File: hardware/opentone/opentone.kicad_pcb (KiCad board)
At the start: 2 copper layers, 161.1 x 143.3 mm, 33 parts, among them J101 POWER, J102 UART, J103 DEBUG, J104 USB, SW101 PWR, SW102 RST, U1 STM32F446RCTx, U101 FSC-BT1035

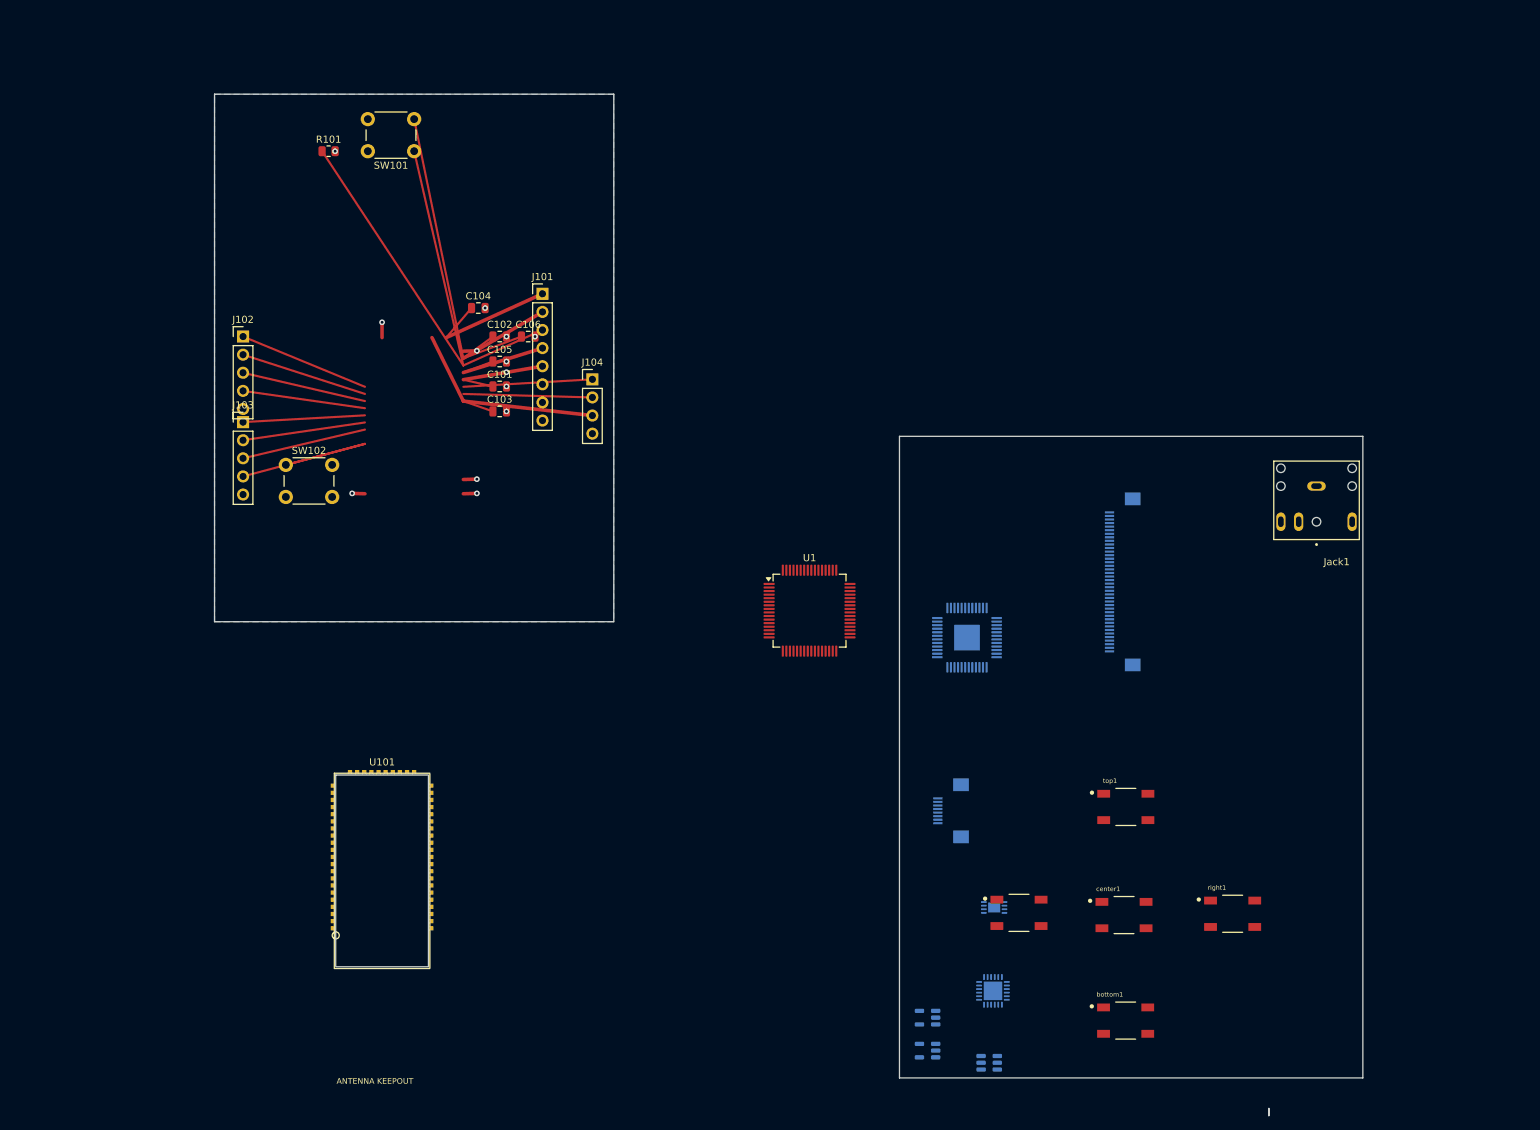
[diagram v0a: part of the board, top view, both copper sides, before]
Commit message: updated buttons and MCU
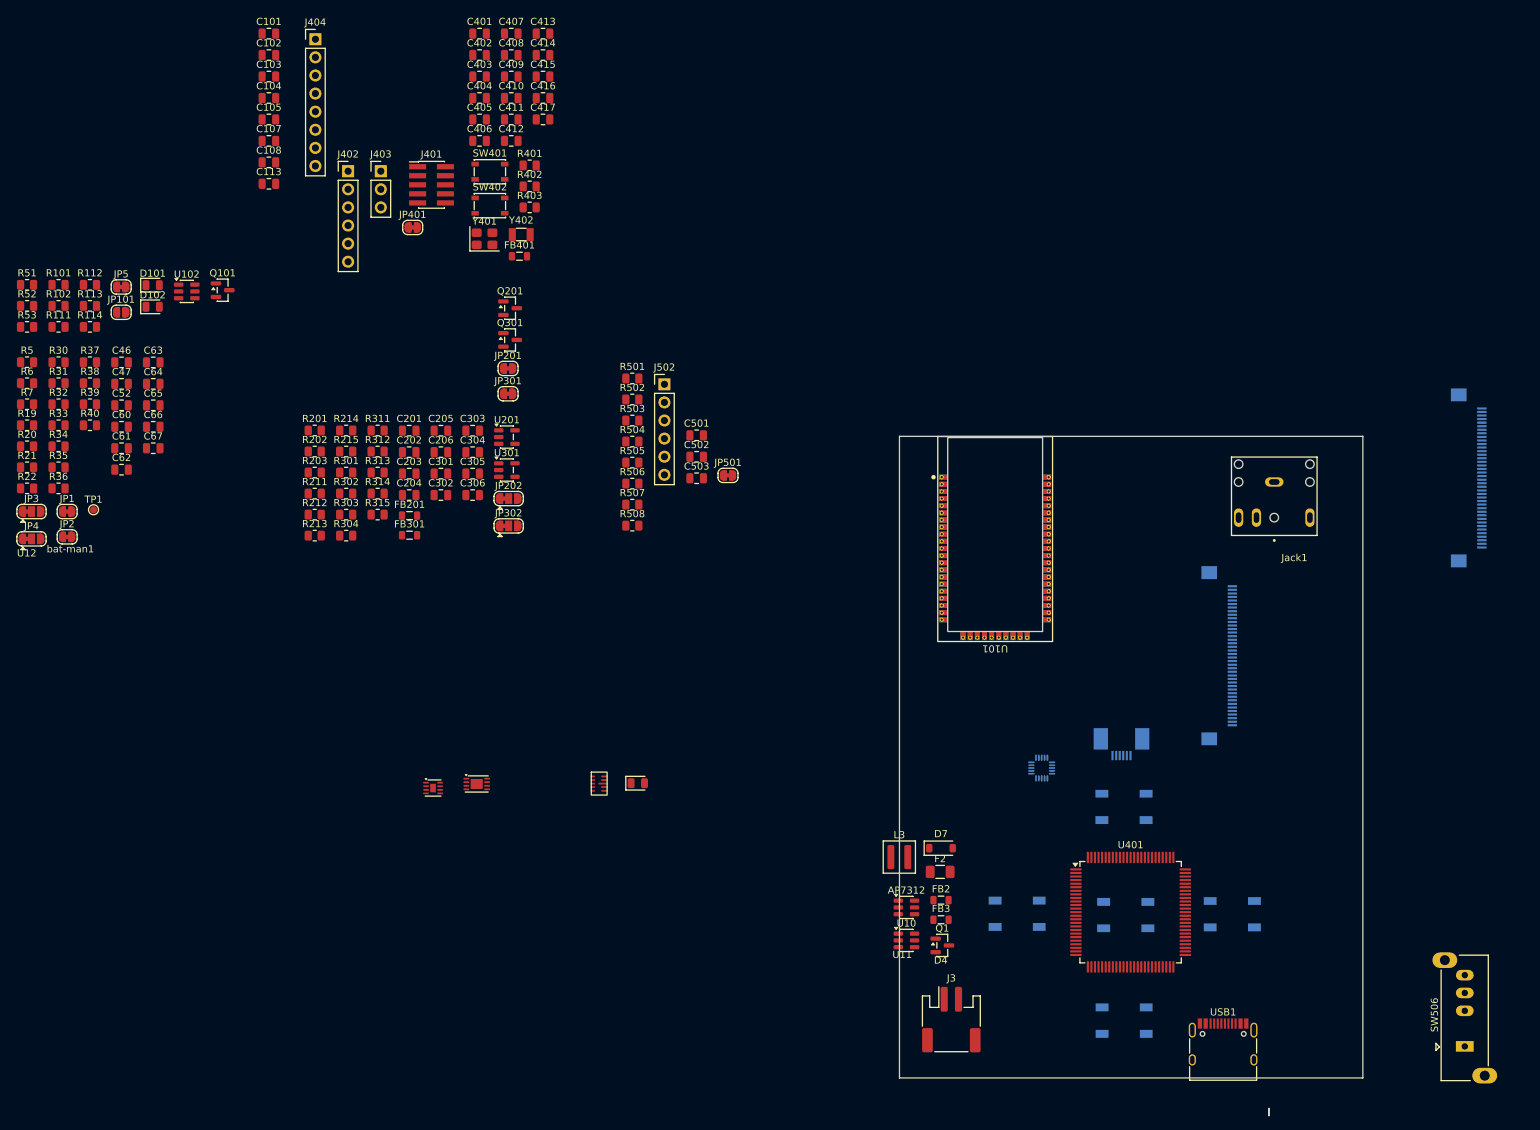
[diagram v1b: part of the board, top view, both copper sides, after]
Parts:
- removed Audiocodec1: VS1063, Package_QFP:LQFP-48-1EP_7x7mm_P0.5mm_EP3.6x3.6mm
- removed Buck-converter2: LM3671, Package_TO_SOT_SMD:TSOT-23-5
- removed C106: 10u, Capacitor_SMD:C_0805_2012Metric
- removed J101: POWER, Connector_PinHeader_2.54mm:PinHeader_1x08_P2.54mm_Vertical
- removed J102: UART, Connector_PinHeader_2.54mm:PinHeader_1x05_P2.54mm_Vertical
- removed J103: DEBUG, Connector_PinHeader_2.54mm:PinHeader_1x05_P2.54mm_Vertical
- removed J104: USB, Connector_PinHeader_2.54mm:PinHeader_1x04_P2.54mm_Vertical
- removed LDO2: MIC5504-3.3YM5, Package_TO_SOT_SMD:SOT-23-5
- removed SW101: PWR, Button_Switch_THT:SW_PUSH_6mm_H4.3mm
- removed SW102: RST, Button_Switch_THT:SW_PUSH_6mm_H4.3mm
- removed S_CONNECTOR1: ~, opentone:Hirose_FH12-40S-0.5SH_1x40-1MP_P0.50mm_Horizontal
- removed U1: STM32F446RCTx, Package_QFP:LQFP-64_10x10mm_P0.5mm
- removed UART_BRIDGE1: CP2102N-Axx-xQFN24, Package_DFN_QFN:QFN-24-1EP_4x4mm_P0.5mm_EP2.6x2.6mm
- removed clickwheel-connector2: ~, Connector_FFC-FPC:Hirose_FH12-8S-0.5SH_1x08-1MP_P0.50mm_Horizontal
- removed left1: SKQGAFE010, opentone:SW_SKQGAFE010
- added C107: 1u, Capacitor_SMD:C_0805_2012Metric, F.Cu at (11.6, 8.55)
- added C108: 1n, Capacitor_SMD:C_0805_2012Metric, F.Cu at (11.6, 11.6)
- added C113: 1u, Capacitor_SMD:C_0805_2012Metric, F.Cu at (11.6, 14.6)
- added C201: 10u, Capacitor_SMD:C_0805_2012Metric, F.Cu at (31.3, 49.2)
- added C202: 100n, Capacitor_SMD:C_0805_2012Metric, F.Cu at (31.3, 52.2)
- added C203: 10u, Capacitor_SMD:C_0805_2012Metric, F.Cu at (31.3, 55.2)
- added C204: 100n, Capacitor_SMD:C_0805_2012Metric, F.Cu at (31.3, 58.2)
- added C205: 100n, Capacitor_SMD:C_0805_2012Metric, F.Cu at (35.8, 49.2)
- added C206: 1u, Capacitor_SMD:C_0805_2012Metric, F.Cu at (35.8, 52.2)
- added C301: 10u, Capacitor_SMD:C_0805_2012Metric, F.Cu at (35.8, 55.2)
- added C302: 100n, Capacitor_SMD:C_0805_2012Metric, F.Cu at (35.8, 58.2)
- added C303: 10u, Capacitor_SMD:C_0805_2012Metric, F.Cu at (40.2, 49.2)
- added C304: 100n, Capacitor_SMD:C_0805_2012Metric, F.Cu at (40.2, 52.2)
- added C305: 100n, Capacitor_SMD:C_0805_2012Metric, F.Cu at (40.2, 55.2)
- added C306: 1u, Capacitor_SMD:C_0805_2012Metric, F.Cu at (40.2, 58.2)
- added C401: 100n, Capacitor_SMD:C_0805_2012Metric, F.Cu at (41.2, -6.50)
- added C402: 100n, Capacitor_SMD:C_0805_2012Metric, F.Cu at (41.2, -3.48)
- added C403: 100n, Capacitor_SMD:C_0805_2012Metric, F.Cu at (41.2, -0.47)
- added C404: 100n, Capacitor_SMD:C_0805_2012Metric, F.Cu at (41.2, 2.54)
- added C405: 100n, Capacitor_SMD:C_0805_2012Metric, F.Cu at (41.2, 5.54)
- added C406: 100n, Capacitor_SMD:C_0805_2012Metric, F.Cu at (41.2, 8.55)
- added C407: 4.7u, Capacitor_SMD:C_0805_2012Metric, F.Cu at (45.6, -6.50)
- added C408: 100n, Capacitor_SMD:C_0805_2012Metric, F.Cu at (45.6, -3.48)
- added C409: 1u, Capacitor_SMD:C_0805_2012Metric, F.Cu at (45.6, -0.47)
- added C410: 100n, Capacitor_SMD:C_0805_2012Metric, F.Cu at (45.6, 2.54)
- added C411: 2.2u, Capacitor_SMD:C_0805_2012Metric, F.Cu at (45.6, 5.54)
- added C412: 2.2u, Capacitor_SMD:C_0805_2012Metric, F.Cu at (45.6, 8.55)
- added C413: 15p, Capacitor_SMD:C_0805_2012Metric, F.Cu at (50.1, -6.50)
- added C414: 15p, Capacitor_SMD:C_0805_2012Metric, F.Cu at (50.1, -3.48)
- added C415: 6.8p, Capacitor_SMD:C_0805_2012Metric, F.Cu at (50.1, -0.47)
- added C416: 6.8p, Capacitor_SMD:C_0805_2012Metric, F.Cu at (50.1, 2.54)
- added C417: 100n, Capacitor_SMD:C_0805_2012Metric, F.Cu at (50.1, 5.54)
- added C46: 4.7uF, Capacitor_SMD:C_0805_2012Metric, F.Cu at (-9.04, 39.6)
- added C47: 4.7uF, Capacitor_SMD:C_0805_2012Metric, F.Cu at (-9.04, 42.6)
- added C501: 100n, Capacitor_SMD:C_0805_2012Metric, F.Cu at (71.6, 49.9)
- added C502: 1u, Capacitor_SMD:C_0805_2012Metric, F.Cu at (71.6, 52.9)
- added C503: 100n, Capacitor_SMD:C_0805_2012Metric, F.Cu at (71.6, 55.9)
- added C52: 1uF, Capacitor_SMD:C_0805_2012Metric, F.Cu at (-9.04, 45.6)
- added C60: 4.7nF, Capacitor_SMD:C_0805_2012Metric, F.Cu at (-9.04, 48.7)
- added C61: 10uF, Capacitor_SMD:C_0805_2012Metric, F.Cu at (-9.04, 51.7)
- added C62: 10uF, Capacitor_SMD:C_0805_2012Metric, F.Cu at (-9.04, 54.7)
- added C63: 22uF, Capacitor_SMD:C_0805_2012Metric, F.Cu at (-4.59, 39.6)
- added C64: 22uF DNP, Capacitor_SMD:C_0805_2012Metric, F.Cu at (-4.59, 42.6)
- added C65: 1uF, Capacitor_SMD:C_0805_2012Metric, F.Cu at (-4.59, 45.6)
- added C66: 10uF, Capacitor_SMD:C_0805_2012Metric, F.Cu at (-4.59, 48.7)
- added C67: 0.1uF, Capacitor_SMD:C_0805_2012Metric, F.Cu at (-4.59, 51.7)
- added D101: LED0, LED_SMD:LED_0805_2012Metric, F.Cu at (-4.67, 28.8)
- added D102: LED1, LED_SMD:LED_0805_2012Metric, F.Cu at (-4.67, 31.8)
- added D4: LED, LED_SMD:LED_0805_2012Metric, F.Cu at (63.4, 98.7)
- added D7: B5819W, Diode_SMD:D_SOD-123, F.Cu at (105.9, 107.8)
- added F2: ASMD1206-075, Fuse:Fuse_1206_3216Metric, F.Cu at (105.8, 111.1)
- added FB2: 600R@100MHz, Inductor_SMD:L_0805_2012Metric, F.Cu at (105.9, 115.1)
- added FB201: 600R/100MHz, Inductor_SMD:L_0805_2012Metric, F.Cu at (31.4, 61.1)
- added FB3: 600R@100MHz, Inductor_SMD:L_0805_2012Metric, F.Cu at (105.9, 117.8)
- added FB301: 600R/100MHz, Inductor_SMD:L_0805_2012Metric, F.Cu at (31.4, 63.9)
- added FB401: 600R@100MHz, Inductor_SMD:L_0805_2012Metric, F.Cu at (46.8, 24.7)
- added J201: LCD_ILI9341_TN_40P, Connector_FFC-FPC:Hirose_FH12-40S-0.5SH_1x40-1MP_P0.50mm_Horizontal, B.Cu at (179.9, 55.8)
- added J3: LiPo JST-PH, Connector_JST:JST_PH_S2B-PH-SM4-TB_1x02-1MP_P2.00mm_Horizontal, F.Cu at (107.4, 131.8)
- added J301: NHD-2.4-240320AF-CSXP, Connector_FFC-FPC:Hirose_FH12-40S-0.5SH_1x40-1MP_P0.50mm_Horizontal, B.Cu at (144.9, 80.8)
- added J401: SWD 2x5 1.27mm, Connector_PinHeader_1.27mm:PinHeader_2x05_P1.27mm_Vertical_SMD, F.Cu at (34.4, 14.7)
- added J402: ST-LINK (Nucleo CN4), Connector_PinHeader_2.54mm:PinHeader_1x06_P2.54mm_Vertical, F.Cu at (22.7, 12.8)
- added J403: Log UART4, Connector_PinHeader_2.54mm:PinHeader_1x03_P2.54mm_Vertical, F.Cu at (27.3, 12.8)
- added J404: Spare GPIO, Connector_PinHeader_2.54mm:PinHeader_1x08_P2.54mm_Vertical, F.Cu at (18.1, -5.71)
- added J501: Wheel FPC 0.5mm, Connector_FFC-FPC:Jushuo_AFC07-S06FCA-00_1x6-1MP_P0.50_Horizontal, B.Cu at (131.2, 93.2)
- added J502: Wheel header, Connector_PinHeader_2.54mm:PinHeader_1x06_P2.54mm_Vertical, F.Cu at (67.1, 42.7)
- added JP1: VBAT drain, Jumper:SolderJumper-2_P1.3mm_Bridged_RoundedPad1.0x1.5mm, F.Cu at (-16.7, 60.5)
- added JP101: BYPASS, Jumper:SolderJumper-2_P1.3mm_Open_RoundedPad1.0x1.5mm, F.Cu at (-9.10, 32.6)
- added JP2: 3V3 drain, Jumper:SolderJumper-2_P1.3mm_Bridged_RoundedPad1.0x1.5mm, F.Cu at (-16.7, 64.1)
- added JP201: TFT1 3V3 drain, Jumper:SolderJumper-2_P1.3mm_Bridged_RoundedPad1.0x1.5mm, F.Cu at (45.2, 40.5)
- added JP202: BL supply, Jumper:SolderJumper-3_P1.3mm_Bridged12_RoundedPad1.0x1.5mm, F.Cu at (45.3, 58.7)
- added JP3: PROG 500mA/100mA, Jumper:SolderJumper-3_P1.3mm_Bridged12_RoundedPad1.0x1.5mm, F.Cu at (-21.7, 60.5)
- added JP301: TFT2 3V3 drain, Jumper:SolderJumper-2_P1.3mm_Bridged_RoundedPad1.0x1.5mm, F.Cu at (45.2, 44.0)
- added JP302: BL supply, Jumper:SolderJumper-3_P1.3mm_Bridged12_RoundedPad1.0x1.5mm, F.Cu at (45.3, 62.6)
- added JP4: AVDD: LDO/filtered 3V3, Jumper:SolderJumper-3_P1.3mm_Bridged12_RoundedPad1.0x1.5mm, F.Cu at (-21.7, 64.4)
- added JP401: MCU drain, Jumper:SolderJumper-2_P1.3mm_Bridged_RoundedPad1.0x1.5mm, F.Cu at (31.8, 20.7)
- added JP5: BT 3V3 drain, Jumper:SolderJumper-2_P1.3mm_Bridged_RoundedPad1.0x1.5mm, F.Cu at (-9.10, 29.0)
- added JP501: MPR121 drain, Jumper:SolderJumper-2_P1.3mm_Bridged_RoundedPad1.0x1.5mm, F.Cu at (76.0, 55.5)
- added L3: 0.47uH XFL4015-471ME, Inductor_SMD:L_Coilcraft_XAL4020-XXX, F.Cu at (100.1, 109.0)
- added Q1: AO3401A, Package_TO_SOT_SMD:SOT-23, F.Cu at (106.1, 121.4)
- added Q101: BSS138, Package_TO_SOT_SMD:SOT-23, F.Cu at (5.13, 29.5)
- added Q201: AO3400A, Package_TO_SOT_SMD:SOT-23, F.Cu at (45.5, 32.0)
- added Q301: AO3400A, Package_TO_SOT_SMD:SOT-23, F.Cu at (45.5, 36.5)
- added R102: 0R, Resistor_SMD:R_0805_2012Metric, F.Cu at (-17.9, 31.7)
- added R111: 2k, Resistor_SMD:R_0805_2012Metric, F.Cu at (-17.9, 34.6)
- added R112: 100k, Resistor_SMD:R_0805_2012Metric, F.Cu at (-13.5, 28.7)
- added R113: 1k, Resistor_SMD:R_0805_2012Metric, F.Cu at (-13.5, 31.7)
- added R114: 1k, Resistor_SMD:R_0805_2012Metric, F.Cu at (-13.5, 34.6)
- added R19: 5.1k, Resistor_SMD:R_0805_2012Metric, F.Cu at (-22.3, 48.4)
- added R20: 5.1k, Resistor_SMD:R_0805_2012Metric, F.Cu at (-22.3, 51.4)
- added R201: 4.7R, Resistor_SMD:R_0805_2012Metric, F.Cu at (18.1, 49.2)
- added R202: 4.7R, Resistor_SMD:R_0805_2012Metric, F.Cu at (18.1, 52.1)
- added R203: 4.7R, Resistor_SMD:R_0805_2012Metric, F.Cu at (18.1, 55.1)
- added R21: 2k, Resistor_SMD:R_0805_2012Metric, F.Cu at (-22.3, 54.3)
- added R211: 100R, Resistor_SMD:R_0805_2012Metric, F.Cu at (18.1, 58.0)
- added R212: 1R 1%, Resistor_SMD:R_0805_2012Metric, F.Cu at (18.1, 61.0)
- added R213: 100k, Resistor_SMD:R_0805_2012Metric, F.Cu at (18.1, 63.9)
- added R214: 56k, Resistor_SMD:R_0805_2012Metric, F.Cu at (22.5, 49.2)
- added R215: 1k 1%, Resistor_SMD:R_0805_2012Metric, F.Cu at (22.5, 52.1)
- added R22: 470, Resistor_SMD:R_0805_2012Metric, F.Cu at (-22.3, 57.3)
- added R30: 0R, Resistor_SMD:R_0805_2012Metric, F.Cu at (-17.9, 39.6)
- added R301: 4.7R, Resistor_SMD:R_0805_2012Metric, F.Cu at (22.5, 55.1)
- added R302: 4.7R, Resistor_SMD:R_0805_2012Metric, F.Cu at (22.5, 58.0)
- added R303: 4.7R, Resistor_SMD:R_0805_2012Metric, F.Cu at (22.5, 61.0)
- added R304: 4.7R, Resistor_SMD:R_0805_2012Metric, F.Cu at (22.5, 63.9)
- added R31: 0R, Resistor_SMD:R_0805_2012Metric, F.Cu at (-17.9, 42.5)
- added R311: 100R, Resistor_SMD:R_0805_2012Metric, F.Cu at (26.9, 49.2)
- added R312: 1R 1%, Resistor_SMD:R_0805_2012Metric, F.Cu at (26.9, 52.1)
- added R313: 100k, Resistor_SMD:R_0805_2012Metric, F.Cu at (26.9, 55.1)
- added R314: 39k, Resistor_SMD:R_0805_2012Metric, F.Cu at (26.9, 58.0)
- added R315: 1k 1%, Resistor_SMD:R_0805_2012Metric, F.Cu at (26.9, 61.0)
- added R32: 1M, Resistor_SMD:R_0805_2012Metric, F.Cu at (-17.9, 45.5)
- added R33: 10k, Resistor_SMD:R_0805_2012Metric, F.Cu at (-17.9, 48.4)
- added R34: 10k, Resistor_SMD:R_0805_2012Metric, F.Cu at (-17.9, 51.4)
- added R35: 100k, Resistor_SMD:R_0805_2012Metric, F.Cu at (-17.9, 54.3)
- added R36: 100k, Resistor_SMD:R_0805_2012Metric, F.Cu at (-17.9, 57.3)
- added R37: 511k, Resistor_SMD:R_0805_2012Metric, F.Cu at (-13.5, 39.6)
- added R38: 91k, Resistor_SMD:R_0805_2012Metric, F.Cu at (-13.5, 42.5)
- added R39: 470k, Resistor_SMD:R_0805_2012Metric, F.Cu at (-13.5, 45.5)
- added R40: 10k, Resistor_SMD:R_0805_2012Metric, F.Cu at (-13.5, 48.4)
- added R401: 10k, Resistor_SMD:R_0805_2012Metric, F.Cu at (48.2, 12.0)
- added R402: 4.7k, Resistor_SMD:R_0805_2012Metric, F.Cu at (48.2, 14.9)
- added R403: 4.7k, Resistor_SMD:R_0805_2012Metric, F.Cu at (48.2, 17.9)
- added R5: 47k, Resistor_SMD:R_0805_2012Metric, F.Cu at (-22.3, 39.6)
- added R501: 10k, Resistor_SMD:R_0805_2012Metric, F.Cu at (62.6, 41.9)
- added R502: 75k 1%, Resistor_SMD:R_0805_2012Metric, F.Cu at (62.6, 44.8)
- added R503: 10k, Resistor_SMD:R_0805_2012Metric, F.Cu at (62.6, 47.8)
- added R504: 10k, Resistor_SMD:R_0805_2012Metric, F.Cu at (62.6, 50.7)
- added R505: 10k, Resistor_SMD:R_0805_2012Metric, F.Cu at (62.6, 53.7)
- added R506: 10k, Resistor_SMD:R_0805_2012Metric, F.Cu at (62.6, 56.6)
- added R507: 10k, Resistor_SMD:R_0805_2012Metric, F.Cu at (62.6, 59.6)
- added R508: 10k, Resistor_SMD:R_0805_2012Metric, F.Cu at (62.6, 62.5)
- added R51: 0R, Resistor_SMD:R_0805_2012Metric, F.Cu at (-22.3, 28.7)
- added R52: 0R, Resistor_SMD:R_0805_2012Metric, F.Cu at (-22.3, 31.7)
- added R53: 0R, Resistor_SMD:R_0805_2012Metric, F.Cu at (-22.3, 34.6)
- added R6: 47k, Resistor_SMD:R_0805_2012Metric, F.Cu at (-22.3, 42.5)
- added R7: 47k, Resistor_SMD:R_0805_2012Metric, F.Cu at (-22.3, 45.5)
- added SW401: RESET, Button_Switch_SMD:SW_SPST_PTS810, F.Cu at (42.6, 12.9)
- added SW402: BOOT0 (DFU), Button_Switch_SMD:SW_SPST_PTS810, F.Cu at (42.6, 17.6)
- added SW505: SKQGAFE010 Left, opentone:SW_SKQGAFE010, B.Cu at (146.8, 117.0)
- added SW506: OFF / HOLD / ON, Button_Switch_THT:SW_Slide_SP3T_Straight_CK_OS103012MU1QP1, F.Cu at (179.4, 135.6)
- added TP1: 3V3_EN, TestPoint:TestPoint_Pad_D1.0mm, F.Cu at (-13.0, 60.3)
- added U10: USBLC6-2SC6, Package_TO_SOT_SMD:SOT-23-6, F.Cu at (101.1, 120.7)
- added U102: TPS22917, Package_TO_SOT_SMD:SOT-23-6, F.Cu at (0.10, 29.7)
- added U11: TPS63802DLAR, opentone:Texas_DLA0010A_VSON-HR-10_2x3mm_P0.5mm, F.Cu at (58.0, 98.7)
- added U12: MAX17048G+T10, Package_DFN_QFN:TDFN-8-1EP_2x2mm_P0.5mm_EP0.8x1.2mm, F.Cu at (34.7, 99.3)
- added U201: MCP6001, Package_TO_SOT_SMD:SOT-23-5, F.Cu at (45.0, 50.1)
- added U301: MCP6001, Package_TO_SOT_SMD:SOT-23-5, F.Cu at (45.0, 54.7)
- added U401: STM32F446VETx, Package_QFP:LQFP-100_14x14mm_P0.5mm, F.Cu at (132.5, 116.7)
- added U501: MPR121QR2, opentone:mpr121qr2, B.Cu at (120.0, 96.5)
- added USB1: USB_C_Receptacle, Connector_USB:USB_C_Receptacle_HRO_TYPE-C-31-M-12, F.Cu at (145.5, 136.4)
- added Y401: 8MHz, Crystal:Crystal_SMD_3225-4Pin_3.2x2.5mm, F.Cu at (41.9, 22.3)
- added Y402: 32.768kHz, Crystal:Crystal_SMD_3215-2Pin_3.2x1.5mm, F.Cu at (47.0, 21.7)
- AP7312: value ~ -> AP7312-1833W6-7; moved to F.Cu
- C101: value 100n -> 10u
- C104, C105: value 100n -> 1u
- bat-man1: moved to F.Cu
- bottom1, center1, right1, top1: moved to B.Cu
- moved U101 98.1 mm to (113.5, 63.8), turned to 180 degrees
- moved bat-man1 74.6 mm to (40.8, 98.8), turned to 0 degrees
- moved C101 59.1 mm to (11.6, -6.50)
- moved C103 57.1 mm to (11.6, -0.47)
- moved C102 51.1 mm to (11.6, -3.48)
- moved C105 46.9 mm to (11.6, 5.54)
- moved R101 42.3 mm to (-17.9, 28.7)
- moved C104 41.6 mm to (11.6, 2.54)
- moved right1 30.2 mm to (116.6, 117.0), turned to 180 degrees
- moved AP7312 24.7 mm to (101.1, 116.1), turned to 0 degrees
- moved Jack1 5.95 mm to (152.7, 56.4)
- moved top1 0.26 mm to (131.6, 102.0), turned to 180 degrees
- moved center1 0.25 mm to (131.8, 117.1), turned to 180 degrees
- moved bottom1 0.21 mm to (131.6, 132.0), turned to 180 degrees
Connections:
- net Net-(C46-Pad2) renamed VBUS
- AP7312 pad 1: 3.3-audio -> /Power/AVDD_LDO
- AP7312 pad 3: +3.3V -> 3V3_EN
- AP7312 pad 4: +3.3V -> 3V3_EN
- AP7312 pad 5: +3.3V -> VSYS
- C101 pad 1: BT_VDD_IO -> /Bluetooth/BT_3V3
- C101 pad 2: BT_GND -> GND
- C102 pad 1: BT_VBAT -> /Bluetooth/BT_3V3
- C102 pad 2: BT_GND -> GND
- C103 pad 1: BT_VCHG -> /Bluetooth/BT_3V3
- C103 pad 2: BT_GND -> GND
- C104 pad 1: BT_3V3 -> /Bluetooth/BT_1V8
- C104 pad 2: BT_GND -> GND
- C105 pad 1: BT_1V8 -> /Bluetooth/BT_3V3_OUT
- C105 pad 2: BT_GND -> GND
- Jack1 pad 10: JACK_SWITCH -> HP1_DET
- R101 pad 1: BT_SYS_CTRL -> /Bluetooth/BT_3V3_IN
- R101 pad 2: BT_GND -> BT_EN
- U101 pad 1: BT_GND -> GND
- U101 pad 10: BT_PIO6 -> unconnected-(U101-PIO6-Pad10)_2
- U101 pad 11: BT_PIO7 -> unconnected-(U101-PIO7-Pad11)
- U101 pad 12: BT_PIO8 -> unconnected-(U101-PIO8-Pad12)
- U101 pad 17: (no net) -> /Bluetooth/BT_LED0
- U101 pad 18: (no net) -> /Bluetooth/BT_LED1
- U101 pad 19: (no net) -> unconnected-(U101-AIO2/LED2-Pad19)_2
- U101 pad 2: (no net) -> unconnected-(U101-AIO4/LED4-Pad2)_1
- U101 pad 20: (no net) -> unconnected-(U101-PIO44-Pad20)_2
- U101 pad 21: (no net) -> unconnected-(U101-PIO41-Pad21)_1
- U101 pad 22: BT_GND -> GND
- U101 pad 23: (no net) -> unconnected-(U101-PIO42-Pad23)_2
- U101 pad 24: (no net) -> unconnected-(U101-PIO43-Pad24)_2
- U101 pad 25: (no net) -> unconnected-(U101-PIO40-Pad25)_2
- U101 pad 26: (no net) -> unconnected-(U101-PIO45-Pad26)_2
- U101 pad 27: (no net) -> unconnected-(U101-PIO20-Pad27)_2
- U101 pad 28: (no net) -> unconnected-(U101-PIO21-Pad28)_2
- U101 pad 29: BT_VCHG -> unconnected-(U101-VCHG_SENSE-Pad29)
- U101 pad 3: (no net) -> unconnected-(U101-AIO5/LED5-Pad3)
- U101 pad 30: (no net) -> unconnected-(U101-NC-Pad30)_1
- U101 pad 31: BT_3V3 -> /Bluetooth/BT_3V3_OUT
- U101 pad 32: BT_GND -> GND
- U101 pad 33: BT_VBAT -> /Bluetooth/BT_3V3
- U101 pad 34: BT_SYS_CTRL -> /Bluetooth/BT_SYS_CTRL
- U101 pad 35: BT_1V8 -> /Bluetooth/BT_1V8
- U101 pad 36: BT_VDD_IO -> /Bluetooth/BT_3V3
- U101 pad 37: BT_USB_DP -> unconnected-(U101-USB_D+-Pad37)
- U101 pad 38: BT_USB_DN -> unconnected-(U101-USB_D--Pad38)
- U101 pad 39: BT_VCHG -> unconnected-(U101-VCHG-Pad39)_2
- U101 pad 4: (no net) -> /Bluetooth/BT_I2S_BCLK
- U101 pad 40: (no net) -> unconnected-(U101-MIC_RP-Pad40)_2
- U101 pad 41: (no net) -> unconnected-(U101-MIC_RN-Pad41)_1
- U101 pad 42: (no net) -> unconnected-(U101-NC-Pad42)
- U101 pad 43: (no net) -> unconnected-(U101-MIC_LP-Pad43)_2
- U101 pad 44: (no net) -> unconnected-(U101-MIC_LN-Pad44)_1
- U101 pad 45: (no net) -> unconnected-(U101-MIC_BIAS-Pad45)_2
- U101 pad 46: (no net) -> unconnected-(U101-NC-Pad46)_1
- U101 pad 47: (no net) -> unconnected-(U101-NC-Pad47)_2
- U101 pad 48: (no net) -> unconnected-(U101-SPK_N-Pad48)_1
- U101 pad 49: (no net) -> unconnected-(U101-SPK_P-Pad49)_1
- U101 pad 5: (no net) -> /Bluetooth/BT_I2S_SDIN
- U101 pad 50: BT_GND -> GND
- U101 pad 51: (no net) -> unconnected-(U101-RF_OUT-Pad51)_1
- U101 pad 52: BT_GND -> GND
- U101 pad 6: (no net) -> unconnected-(U101-PCM_OUT/PIO18-Pad6)
- U101 pad 7: (no net) -> /Bluetooth/BT_I2S_LRCK
- U101 pad 9: (no net) -> unconnected-(U101-PCM_MCLK_OUT/PIO15-Pad9)_1
- bat-man1 pad 5: Net-(D4-Pad1) -> /Power/STAT
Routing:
- net BT_SYS_CTRL: track 79.0 -> 0.00 mm
- net BT_VBAT: track 61.0 -> 0.00 mm
- net BT_VCHG: track 32.5 -> 0.00 mm
- net BT_RESET: track 29.2 -> 0.00 mm
- net BT_3V3: track 20.3 -> 0.00 mm
- net BT_RTS: track 18.5 -> 0.00 mm
- net BT_USB_DP: track 18.1 -> 0.00 mm
- net BT_USB_DN: track 18.1 -> 0.00 mm
- net BT_CTS: track 18.0 -> 0.00 mm
- net BT_PIO6: track 17.6 -> 0.00 mm
- net BT_RX: track 17.6 -> 0.00 mm
- net BT_PIO7: track 17.3 -> 0.00 mm
- net BT_TX: track 17.3 -> 0.00 mm
- net BT_PIO8: track 17.1 -> 0.00 mm
- net BT_1V8: track 16.0 -> 0.00 mm
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- removed copper zone on B.Cu, net BT_GND
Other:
- board size 161.1 x 143.3 mm -> 65 x 95.3 mm

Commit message: added sd card, haptic, updated old parts and set a datasheet and MPN to all parts
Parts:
- removed Clickwheel1: ~, opentone:clickwheel_1
- removed MPR1: MPR121QR2, opentone:mpr121qr2
- removed SCREEN1: ~, opentone:nhd-2.4-240320cf-ctxif
- removed bottom1, center1, right1, top1: SKQGAFE010, opentone:SW_SKQGAFE010
- removed clickwheel-connector1: ~, Connector_FFC-FPC:Hirose_FH12-8S-0.5SH_1x08-1MP_P0.50mm_Horizontal
- added C29: 10nF, Capacitor_SMD:C_0603_1608Metric, F.Cu at (230.8, 62.5)
- added C3: 10nF, Capacitor_SMD:C_0603_1608Metric, F.Cu at (230.8, 60.0)
- added C30: 100nF, Capacitor_SMD:C_0603_1608Metric, F.Cu at (230.8, 65.0)
- added C31: 100nF, Capacitor_SMD:C_0603_1608Metric, F.Cu at (230.8, 67.5)
- added C32: 100nF, Capacitor_SMD:C_0603_1608Metric, F.Cu at (230.8, 70.1)
- added C33: 10uF, Capacitor_SMD:C_0603_1608Metric, F.Cu at (230.8, 72.6)
- added C34: 1uF, Capacitor_SMD:C_0603_1608Metric, F.Cu at (230.8, 75.1)
- added C35: 10uF, Capacitor_SMD:C_0603_1608Metric, F.Cu at (230.8, 77.6)
- added C36: 18pF, Capacitor_SMD:C_0603_1608Metric, F.Cu at (230.8, 80.1)
- added C37: 100nF, Capacitor_SMD:C_0603_1608Metric, F.Cu at (234.8, 60.0)
- added C38: 18pF, Capacitor_SMD:C_0603_1608Metric, F.Cu at (234.8, 62.5)
- added C39: 100nF, Capacitor_SMD:C_0603_1608Metric, F.Cu at (234.8, 65.0)
- added C40: 10uF, Capacitor_SMD:C_0603_1608Metric, F.Cu at (234.8, 67.5)
- added C41: 100nF, Capacitor_SMD:C_0603_1608Metric, F.Cu at (234.8, 70.1)
- added C42: 100nF, Capacitor_SMD:C_0603_1608Metric, F.Cu at (234.8, 72.6)
- added C43: 100nF, Capacitor_SMD:C_0603_1608Metric, F.Cu at (234.8, 75.1)
- added C44: 100nF, Capacitor_SMD:C_0603_1608Metric, F.Cu at (234.8, 77.6)
- added C45: 100nF, Capacitor_SMD:C_0603_1608Metric, F.Cu at (234.8, 80.1)
- added C601: 100n, Capacitor_SMD:C_0603_1608Metric, F.Cu at (247.6, 31.8)
- added C602: 4.7u, Capacitor_SMD:C_0603_1608Metric, F.Cu at (247.6, 34.3)
- added C603: 1u, Capacitor_SMD:C_0603_1608Metric, F.Cu at (247.6, 36.8)
- added C604: 1n, Capacitor_SMD:C_0603_1608Metric, F.Cu at (247.6, 39.3)
- added C605: 10u, Capacitor_SMD:C_0603_1608Metric, F.Cu at (247.6, 41.8)
- added C606: 100n, Capacitor_SMD:C_0603_1608Metric, F.Cu at (247.6, 44.3)
- added C9: 47nF, Capacitor_SMD:C_1206_3216Metric, F.Cu at (247.7, 71.8)
- added J601: DM3AT-SF-PEJM5, Connector_Card:microSD_HC_Hirose_DM3AT-SF-PEJM5, F.Cu at (237.2, 39.8)
- added JP601: PSRAM 3V3 drain, Jumper:SolderJumper-2_P1.3mm_Bridged_RoundedPad1.0x1.5mm, F.Cu at (247.7, 47.3)
- added JP602: SD 3V3 drain, Jumper:SolderJumper-2_P1.3mm_Bridged_RoundedPad1.0x1.5mm, F.Cu at (247.7, 50.9)
- added JP603: BYPASS, Jumper:SolderJumper-2_P1.3mm_Open_RoundedPad1.0x1.5mm, F.Cu at (247.7, 54.4)
- added R13: 10, Resistor_SMD:R_0603_1608Metric, F.Cu at (238.8, 65.0)
- added R14: 20, Resistor_SMD:R_0603_1608Metric, F.Cu at (238.8, 67.5)
- added R16: 100k, Resistor_SMD:R_0603_1608Metric, F.Cu at (238.8, 70.1)
- added R17: 100k, Resistor_SMD:R_0603_1608Metric, F.Cu at (238.8, 72.6)
- added R18: 1M, Resistor_SMD:R_0603_1608Metric, F.Cu at (238.8, 75.1)
- added R2: 20, Resistor_SMD:R_0603_1608Metric, F.Cu at (238.8, 60.0)
- added R3: 100K, Resistor_SMD:R_0603_1608Metric, F.Cu at (238.8, 62.5)
- added R41: 100k, Resistor_SMD:R_0603_1608Metric, F.Cu at (238.8, 77.6)
- added R42: 100k, Resistor_SMD:R_0603_1608Metric, F.Cu at (238.8, 80.1)
- added R43: 100k, Resistor_SMD:R_0603_1608Metric, F.Cu at (242.9, 60.0)
- added R44: 100k, Resistor_SMD:R_0603_1608Metric, F.Cu at (242.9, 62.5)
- added R45: 100k, Resistor_SMD:R_0603_1608Metric, F.Cu at (242.9, 65.0)
- added R46: 100k, Resistor_SMD:R_0603_1608Metric, F.Cu at (242.9, 67.5)
- added R47: 100k, Resistor_SMD:R_0603_1608Metric, F.Cu at (242.9, 70.1)
- added R601: 0R, Resistor_SMD:R_0603_1608Metric, F.Cu at (251.6, 31.8)
- added R602: 0R, Resistor_SMD:R_0603_1608Metric, F.Cu at (251.6, 34.3)
- added R603: 0R, Resistor_SMD:R_0603_1608Metric, F.Cu at (251.6, 36.8)
- added R604: 0R, Resistor_SMD:R_0603_1608Metric, F.Cu at (251.6, 39.3)
- added R605: 0R, Resistor_SMD:R_0603_1608Metric, F.Cu at (251.6, 41.8)
- added R606: 0R, Resistor_SMD:R_0603_1608Metric, F.Cu at (251.6, 44.3)
- added R607: 10k, Resistor_SMD:R_0603_1608Metric, F.Cu at (255.6, 31.8)
- added R610: 100k, Resistor_SMD:R_0603_1608Metric, F.Cu at (255.6, 34.3)
- added R611: 0R, Resistor_SMD:R_0603_1608Metric, F.Cu at (255.6, 36.8)
- added R612: 0R, Resistor_SMD:R_0603_1608Metric, F.Cu at (255.6, 39.3)
- added R613: 0R, Resistor_SMD:R_0603_1608Metric, F.Cu at (255.6, 41.8)
- added R614: 0R, Resistor_SMD:R_0603_1608Metric, F.Cu at (255.6, 44.3)
- added R615: 47k, Resistor_SMD:R_0603_1608Metric, F.Cu at (259.6, 31.8)
- added R616: 47k, Resistor_SMD:R_0603_1608Metric, F.Cu at (259.6, 34.3)
- added R617: 47k, Resistor_SMD:R_0603_1608Metric, F.Cu at (259.6, 36.8)
- added R618: 47k, Resistor_SMD:R_0603_1608Metric, F.Cu at (259.6, 39.3)
- added R619: 47k, Resistor_SMD:R_0603_1608Metric, F.Cu at (259.6, 41.8)
- added R620: 100k, Resistor_SMD:R_0603_1608Metric, F.Cu at (259.6, 44.3)
- added SW501: SKQGAFE010 Center, opentone:SW_SKQGAFE010, F.Cu at (222.1, 34.0)
- added SW502: SKQGAFE010 Top, opentone:SW_SKQGAFE010, F.Cu at (222.1, 41.1)
- added SW503: SKQGAFE010 Right, opentone:SW_SKQGAFE010, F.Cu at (222.1, 48.1)
- added SW504: SKQGAFE010 Bottom, opentone:SW_SKQGAFE010, F.Cu at (222.1, 55.2)
- added U601: APS6404L-3SQN-SN, Package_SO:SOIC-8_3.9x4.9mm_P1.27mm, F.Cu at (254.1, 48.9)
- added U602: TPS22917, Package_TO_SOT_SMD:SOT-23-6, F.Cu at (252.5, 54.5)
- added VS1: VS1053B-L, Package_QFP:LQFP-48_7x7mm_P0.5mm, F.Cu at (250.5, 64.4)
- added Y1: 12.288MHz, Crystal:Crystal_SMD_3225-4Pin_3.2x2.5mm, F.Cu at (247.5, 75.7)
- C101, C102, C103, C104, C105, C107, C108, C113, C201, C202, C203, C204, C205, C206, C301, C302, C303, C304, C305, C306, C401, C402, C403, C404, C405, C406, C407, C408, C409, C410, C411, C412, C413, C414, C415, C416, C417, C501, C502, C503, C52, C60, C65, C66, C67: footprint Capacitor_SMD:C_0805_2012Metric -> Capacitor_SMD:C_0603_1608Metric
- D101, D102, D4: footprint LED_SMD:LED_0805_2012Metric -> LED_SMD:LED_0603_1608Metric
- FB2, FB201, FB3, FB301, FB401: footprint Inductor_SMD:L_0805_2012Metric -> Inductor_SMD:L_0603_1608Metric
- Jack1: value SJ1-3524NG -> SJ-43515TS-SMT-TR; footprint opentone:CUI_SJ1-3524NG -> opentone:CUI_SJ-43515TS-SMT-TR
- R101, R102, R111, R112, R113, R114, R19, R20, R201, R202, R203, R21, R211, R212, R213, R214, R215, R22, R30, R301, R302, R303, R304, R31, R311, R312, R313, R314, R315, R32, R33, R34, R35, R36, R37, R38, R39, R40, R401, R402, R403, R5, R501, R502, R503, R504, R505, R506, R507, R508, R51, R52, R53, R6, R7: footprint Resistor_SMD:R_0805_2012Metric -> Resistor_SMD:R_0603_1608Metric
- SW506: footprint Button_Switch_THT:SW_Slide_SP3T_Straight_CK_OS103012MU1QP1 -> Button_Switch_SMD:SW_SP3T_PCM13
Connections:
- SW506 pad 2: GND -> LOCK_SW
- SW506 pad 3: LOCK_SW -> GND
